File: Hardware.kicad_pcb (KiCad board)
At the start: 2 copper layers, 30.5 x 24 mm, 0 parts

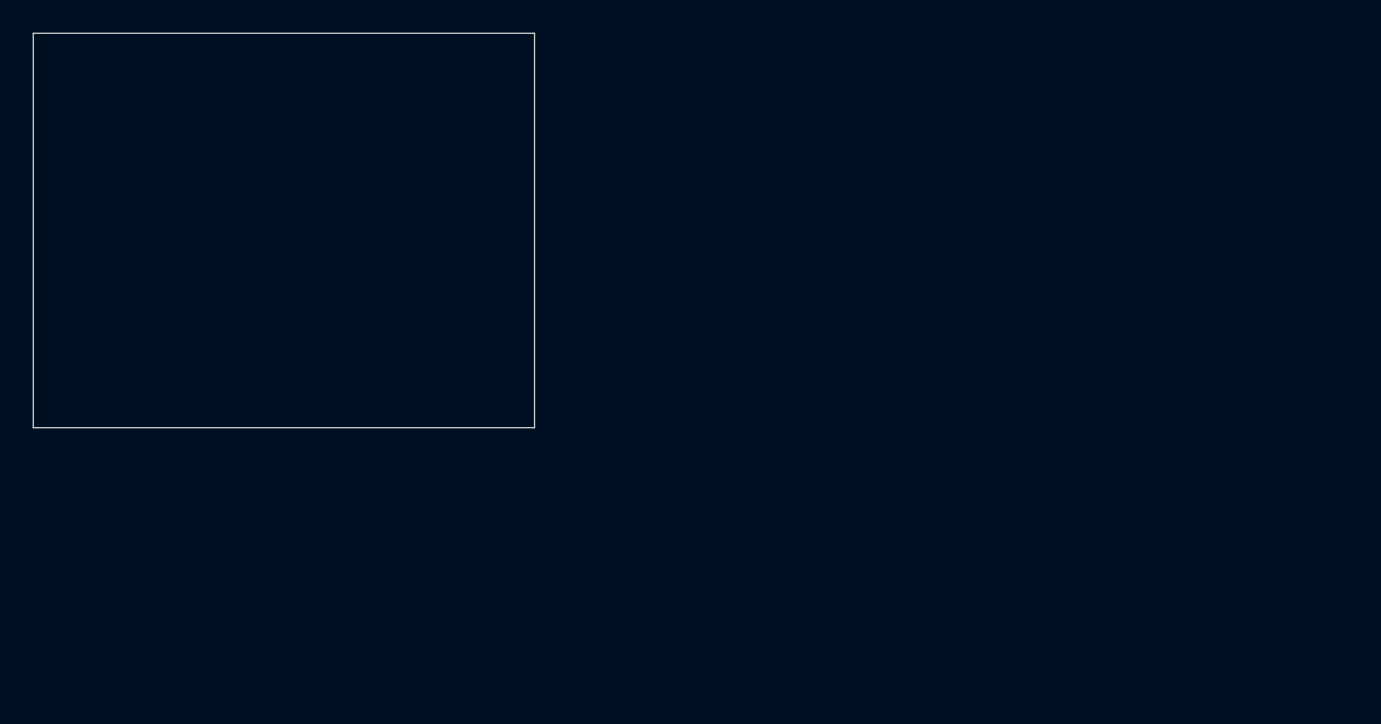
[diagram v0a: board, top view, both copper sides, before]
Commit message: added psu and formated board outline
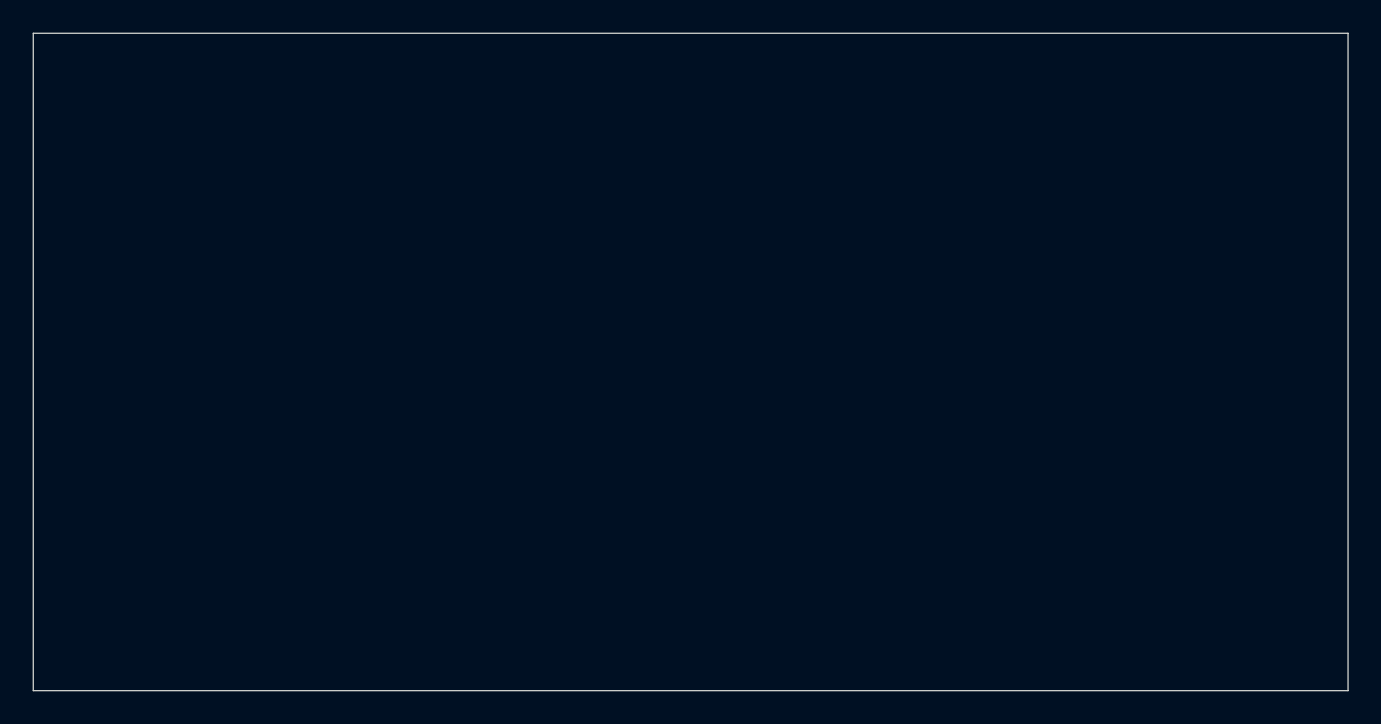
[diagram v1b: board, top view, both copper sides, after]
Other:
- board size 30.5 x 24 mm -> 80 x 40 mm
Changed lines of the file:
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@@
 	(gr_rect
 		(start 35.5 50)
-		(end 66 74)
+		(end 115.5 90)
 		(stroke
 			(width 0.05)

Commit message: finelized scematics
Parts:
- added BT1: Battery_Cell, Battery:BatteryHolder_Seiko_MS621F, F.Cu at (244.6, 128.6)
- added C1: 0.1uF, Capacitor_SMD:C_0805_2012Metric, F.Cu at (174.9, 100.5)
- added C10: NC, Capacitor_SMD:C_0805_2012Metric, F.Cu at (270.3, 86.3)
- added C11: NC, Capacitor_SMD:C_0805_2012Metric, F.Cu at (270.3, 89.3)
- added C14: 10uF, Capacitor_SMD:C_1206_3216Metric, F.Cu at (260.4, 86.4)
- added C17: 100pF, Capacitor_SMD:C_0805_2012Metric, F.Cu at (270.3, 92.3)
- added C18: 100pF, Capacitor_SMD:C_0805_2012Metric, F.Cu at (270.1, 111.4)
- added C19: 100pF, Capacitor_SMD:C_0805_2012Metric, F.Cu at (270.1, 114.4)
- added C2: 10uF, Capacitor_SMD:C_1206_3216Metric, F.Cu at (213.7, 100.7)
- added C20: 4.7uF, Capacitor_SMD:C_0805_2012Metric, F.Cu at (270.1, 117.4)
- added C21: 10uF, Capacitor_SMD:C_1206_3216Metric, F.Cu at (260.4, 89.8)
- added C22: 0.1uF, Capacitor_SMD:C_0805_2012Metric, F.Cu at (174.9, 112.6)
- added C23: 0.1uF, Capacitor_SMD:C_0805_2012Metric, F.Cu at (174.9, 115.6)
- added C24: 100pF, Capacitor_SMD:C_0805_2012Metric, F.Cu at (274.8, 86.3)
- added C25: 10uF, Capacitor_SMD:C_1206_3216Metric, F.Cu at (260.4, 93.1)
- added C26: 100pF, Capacitor_SMD:C_0805_2012Metric, F.Cu at (274.8, 89.3)
- added C27: 10uF, Capacitor_SMD:C_1206_3216Metric, F.Cu at (192.3, 132.1)
- added C28: 100pF, Capacitor_SMD:C_0805_2012Metric, F.Cu at (191.7, 138.6)
- added C29: 10uF, Capacitor_SMD:C_1206_3216Metric, F.Cu at (192.3, 135.4)
- added C3: 100pF, Capacitor_SMD:C_0805_2012Metric, F.Cu at (174.9, 103.5)
- added C30: 100pF, Capacitor_SMD:C_0805_2012Metric, F.Cu at (191.7, 141.6)
- added C31: 10uF, Capacitor_SMD:C_1206_3216Metric, F.Cu at (260.4, 96.5)
- added C32: 100pF, Capacitor_SMD:C_0805_2012Metric, F.Cu at (274.8, 92.3)
- added C33: 10uF, Capacitor_SMD:C_1206_3216Metric, F.Cu at (260.4, 99.8)
- added C34: 100pF, Capacitor_SMD:C_0805_2012Metric, F.Cu at (279.2, 86.3)
- added C35: 10uF, Capacitor_SMD:C_1206_3216Metric, F.Cu at (253.6, 127.5)
- added C36: 100pF, Capacitor_SMD:C_0805_2012Metric, F.Cu at (259.1, 121.3)
- added C37: 10uF, Capacitor_SMD:C_1206_3216Metric, F.Cu at (253.6, 130.9)
- added C38: 100pF, Capacitor_SMD:C_0805_2012Metric, F.Cu at (259.1, 124.3)
- added C39: 4.7uF, Capacitor_SMD:C_0805_2012Metric, F.Cu at (215.5, 123.6)
- added C4: 22uF, Capacitor_SMD:C_0603_1608Metric, F.Cu at (194.3, 100.3)
- added C40: 4.7uF, Capacitor_SMD:C_0805_2012Metric, F.Cu at (215.5, 126.6)
- added C41: 22uF, Capacitor_SMD:C_0603_1608Metric, F.Cu at (266.2, 58.0)
- added C42: 100pF, Capacitor_SMD:C_0805_2012Metric, F.Cu at (174.9, 118.6)
- added C43: 22uF, Capacitor_SMD:C_0603_1608Metric, F.Cu at (266.2, 60.5)
- added C44: 100pF, Capacitor_SMD:C_0805_2012Metric, F.Cu at (279.2, 89.3)
- added C45: 22uF, Capacitor_SMD:C_0603_1608Metric, F.Cu at (266.2, 63.0)
- added C46: 0.1uF, Capacitor_SMD:C_0805_2012Metric, F.Cu at (215.5, 129.6)
- added C47: 470pF, Capacitor_SMD:C_0603_1608Metric, F.Cu at (203.3, 123.3)
- added C48: 470pF, Capacitor_SMD:C_0603_1608Metric, F.Cu at (203.3, 125.8)
- added C49: 10uF, Capacitor_SMD:C_1206_3216Metric, F.Cu at (260.4, 103.2)
- added C5: 0.1uF, Capacitor_SMD:C_0805_2012Metric, F.Cu at (174.9, 106.5)
- added C50: 100pF, Capacitor_SMD:C_0805_2012Metric, F.Cu at (279.2, 92.3)
- added C51: 1uF, Capacitor_SMD:C_0603_1608Metric, F.Cu at (203.3, 128.4)
- added C6: 22uF, Capacitor_SMD:C_0603_1608Metric, F.Cu at (274.3, 114.7)
- added C7: 0.1uF, Capacitor_SMD:C_0805_2012Metric, F.Cu at (270.1, 108.4)
- added C8: 10uF, Capacitor_SMD:C_1206_3216Metric, F.Cu at (213.7, 104.0)
- added C9: 100pF, Capacitor_SMD:C_0805_2012Metric, F.Cu at (174.9, 109.5)
- added D1: LED, Capacitor_SMD:C_0603_1608Metric, F.Cu at (248.4, 125.7)
- added D10: BZV55B5V1, Diode_SMD:D_MiniMELF, F.Cu at (219.7, 100.7)
- added D12: 1N5819, Diode_THT:D_DO-41_SOD81_P10.16mm_Horizontal, F.Cu at (215.2, 139.8)
- added D2: 1N4148, Diode_THT:D_DO-35_SOD27_P7.62mm_Horizontal, F.Cu at (237.0, 134.6)
- added D3: PESD1CAN, Package_TO_SOT_SMD:SOT-23-3, F.Cu at (278.9, 122.5)
- added D4: LED, Capacitor_SMD:C_0603_1608Metric, F.Cu at (266.2, 65.5)
- added D5: LED, Capacitor_SMD:C_0603_1608Metric, F.Cu at (266.2, 68.0)
- added D6: BZV55B5V1, Diode_SMD:D_MiniMELF, F.Cu at (277.2, 82.0)
- added D7: LED, Capacitor_SMD:C_0603_1608Metric, F.Cu at (203.3, 130.9)
- added D8: LED, Capacitor_SMD:C_0603_1608Metric, F.Cu at (203.3, 133.4)
- added H1: MountingHole_Pad, MountingHole:MountingHole_3.2mm_M3_DIN965_Pad, F.Cu at (225.3, 60.3)
- added H2: MountingHole_Pad, MountingHole:MountingHole_3.2mm_M3_DIN965_Pad, F.Cu at (225.3, 67.4)
- added H3: MountingHole_Pad, MountingHole:MountingHole_3.2mm_M3_DIN965_Pad, F.Cu at (225.3, 74.6)
- added H4: MountingHole_Pad, MountingHole:MountingHole_3.2mm_M3_DIN965_Pad, F.Cu at (225.3, 81.7)
- added J1: Conn_01x06_Socket, Connector_PinHeader_2.54mm:PinHeader_1x06_P2.54mm_Vertical, F.Cu at (179.5, 101.3)
- added J2: JAE_SIM_Card_SF72S006, Connector_JAE:JAE_SIM_Card_SF72S006, F.Cu at (242.9, 90.7)
- added J3: Conn_Coaxial, Connector_Coaxial:U.FL_Molex_MCRF_73412-0110_Vertical, F.Cu at (253.8, 122.8)
- added J4: Conn_Coaxial, Connector_Coaxial:U.FL_Molex_MCRF_73412-0110_Vertical, F.Cu at (277.0, 77.3)
- added J5: Conn_01x05_Socket, Connector_PinHeader_2.54mm:PinHeader_1x05_P2.54mm_Vertical, F.Cu at (198.7, 101.3)
- added J6: Micro_SD_Card, Connector_Card:microSD_HC_Hirose_DM3BT-DSF-PEJS, F.Cu at (181.1, 131.4)
- added J9: Battery, Connector_JST:JST_PH_S2B-PH-SM4-TB_1x02-1MP_P2.00mm_Horizontal, F.Cu at (206.4, 140.3)
- added L1: 27uH, Inductor_SMD:L_0805_2012Metric, F.Cu at (253.1, 133.9)
- added L4: EPCO B82787C0513, EPCO_B82787C0513:EPCO B82787C0513, F.Cu at (278.8, 116.8)
- added L6: 220uH, Inductor_SMD:L_7.3x7.3_H4.5, F.Cu at (222.5, 126.5)
- added Q1: BC849, Package_TO_SOT_SMD:SOT-23, F.Cu at (203.4, 109.7)
- added Q2: BC849, Package_TO_SOT_SMD:SOT-23, F.Cu at (203.4, 114.4)
- added Q3: MMBT3904, Package_TO_SOT_SMD:SOT-23, F.Cu at (265.7, 87.2)
- added Q4: BC849, Package_TO_SOT_SMD:SOT-23, F.Cu at (265.7, 91.8)
- added Q5: MMBT3904, Package_TO_SOT_SMD:SOT-23, F.Cu at (265.7, 96.4)
- added Q6: MMBT3904, Package_TO_SOT_SMD:SOT-23, F.Cu at (265.7, 101.0)
- added R1: 10K, Resistor_SMD:R_0603_1608Metric, F.Cu at (194.3, 102.8)
- added R10: 60R, Resistor_SMD:R_0603_1608Metric, F.Cu at (274.3, 117.2)
- added R11: 60R, Resistor_SMD:R_0603_1608Metric, F.Cu at (274.3, 119.7)
- added R12: 120R, Resistor_SMD:R_0603_1608Metric, F.Cu at (248.4, 133.2)
- added R13: R33, Resistor_SMD:R_0603_1608Metric, F.Cu at (266.2, 70.5)
- added R17: 51R, Resistor_SMD:R_0603_1608Metric, F.Cu at (266.2, 73.0)
- added R18: 100K, Resistor_SMD:R_0603_1608Metric, F.Cu at (270.2, 58.0)
- added R19: 4K7, Resistor_SMD:R_0603_1608Metric, F.Cu at (270.2, 60.5)
- added R2: 1K, Resistor_SMD:R_0603_1608Metric, F.Cu at (207.3, 123.3)
- added R20: 4K7, Resistor_SMD:R_0603_1608Metric, F.Cu at (270.2, 63.0)
- added R21: 1k18, Resistor_SMD:R_0603_1608Metric, F.Cu at (207.3, 133.4)
- added R22: 10K, Resistor_SMD:R_0603_1608Metric, F.Cu at (194.3, 110.3)
- added R23: 3K9, Resistor_SMD:R_0603_1608Metric, F.Cu at (194.3, 112.8)
- added R24: 22R, Resistor_SMD:R_0603_1608Metric, F.Cu at (270.2, 65.5)
- added R25: 22R, Resistor_SMD:R_0603_1608Metric, F.Cu at (270.2, 68.0)
- added R26: 22R, Resistor_SMD:R_0603_1608Metric, F.Cu at (270.2, 70.5)
- added R29: 0.33R, Resistor_SMD:R_0603_1608Metric, F.Cu at (211.3, 123.3)
- added R3: 10K, Resistor_SMD:R_0603_1608Metric, F.Cu at (194.3, 105.3)
- added R30: 3K3, Resistor_SMD:R_0603_1608Metric, F.Cu at (211.3, 125.8)
- added R31: 1K2, Resistor_SMD:R_0603_1608Metric, F.Cu at (211.3, 128.4)
- added R4: 10K, Resistor_SMD:R_0603_1608Metric, F.Cu at (194.3, 107.8)
- added R41: 4K7, Resistor_SMD:R_0603_1608Metric, F.Cu at (270.2, 73.0)
- added R42: 47K, Resistor_SMD:R_0603_1608Metric, F.Cu at (274.2, 58.0)
- added R43: 51R, Resistor_SMD:R_0603_1608Metric, F.Cu at (274.2, 60.5)
- added R44: 1K, Resistor_SMD:R_0603_1608Metric, F.Cu at (274.2, 63.0)
- added R45: 1K, Resistor_SMD:R_0603_1608Metric, F.Cu at (274.2, 65.5)
- added R46: 4K7, Resistor_SMD:R_0603_1608Metric, F.Cu at (274.2, 68.0)
- added R47: 4K7, Resistor_SMD:R_0603_1608Metric, F.Cu at (274.2, 70.5)
- added R48: 100K, Resistor_SMD:R_0603_1608Metric, F.Cu at (274.2, 73.0)
- added R49: 4K7, Resistor_SMD:R_0603_1608Metric, F.Cu at (278.2, 58.0)
- added R5: 1K, Resistor_SMD:R_0603_1608Metric, F.Cu at (207.3, 125.8)
- added R50: 4K7, Resistor_SMD:R_0603_1608Metric, F.Cu at (278.2, 60.5)
- added R51: 22K, Resistor_SMD:R_0603_1608Metric, F.Cu at (278.2, 63.0)
- added R52: 10K, Resistor_SMD:R_0603_1608Metric, F.Cu at (278.2, 65.5)
- added R6: 10K, Resistor_SMD:R_0603_1608Metric, F.Cu at (207.3, 128.4)
- added R7: 1k13, Resistor_SMD:R_0603_1608Metric, F.Cu at (207.3, 130.9)
- added R8: 22R, Resistor_SMD:R_0603_1608Metric, F.Cu at (248.4, 128.2)
- added R9: 1K, Resistor_SMD:R_0603_1608Metric, F.Cu at (248.4, 130.7)
- added SW1: SW_Push, Button_Switch_THT:SW_PUSH_6mm, F.Cu at (183.8, 101.0)
- added SW3: SW_Push, Button_Switch_THT:SW_PUSH_6mm, F.Cu at (183.8, 109.6)
- added TP1: TestPoint, TestPoint:TestPoint_Pad_D2.0mm, F.Cu at (265.6, 109.1)
- added TP10: TestPoint, TestPoint:TestPoint_Pad_D2.0mm, F.Cu at (265.6, 122.8)
- added TP11: TestPoint, TestPoint:TestPoint_Pad_D2.0mm, F.Cu at (255.3, 87.0)
- added TP12: TestPoint, TestPoint:TestPoint_Pad_D2.0mm, F.Cu at (255.3, 91.6)
- added TP13: TestPoint, TestPoint:TestPoint_Pad_D2.0mm, F.Cu at (231.2, 63.5)
- added TP14: TestPoint, TestPoint:TestPoint_Pad_D2.0mm, F.Cu at (231.2, 68.1)
- added TP15: TestPoint, TestPoint:TestPoint_Pad_D2.0mm, F.Cu at (231.2, 72.6)
- added TP17: TestPoint, TestPoint:TestPoint_Pad_D2.0mm, F.Cu at (255.3, 96.1)
- added TP18: TestPoint, TestPoint:TestPoint_Pad_D2.0mm, F.Cu at (196.2, 139.4)
- added TP19: TestPoint, TestPoint:TestPoint_Pad_D2.0mm, F.Cu at (258.7, 132.7)
- added TP2: TestPoint, TestPoint:TestPoint_Pad_D2.0mm, F.Cu at (250.8, 87.0)
- added TP20: TestPoint, TestPoint:TestPoint_Pad_D2.0mm, F.Cu at (243.5, 147.9)
- added TP21: TestPoint, TestPoint:TestPoint_Pad_D2.0mm, F.Cu at (243.5, 152.5)
- added TP3: TestPoint, TestPoint:TestPoint_Pad_D2.0mm, F.Cu at (258.7, 128.1)
- added TP4: TestPoint, TestPoint:TestPoint_Pad_D2.0mm, F.Cu at (265.6, 113.7)
- added TP5: TestPoint, TestPoint:TestPoint_Pad_D2.0mm, F.Cu at (265.6, 118.2)
- added TP6: TestPoint, TestPoint:TestPoint_Pad_D2.0mm, F.Cu at (231.2, 59.0)
- added TP7: TestPoint, TestPoint:TestPoint_Pad_D2.0mm, F.Cu at (250.8, 91.6)
- added TP8: TestPoint, TestPoint:TestPoint_Pad_D2.0mm, F.Cu at (250.8, 96.1)
- added TP9: TestPoint, TestPoint:TestPoint_Pad_D2.0mm, F.Cu at (250.8, 100.7)
- added U1: ESP32-WROOM-32, RF_Module:ESP32-WROOM-32, F.Cu at (197.2, 88.0)
- added U10: MIC29302AWD, Package_TO_SOT_SMD:TO-252-5_TabPin3, F.Cu at (275.0, 97.8)
- added U11: AMS1117-3.3, Package_TO_SOT_SMD:SOT-223-3_TabPin2, F.Cu at (255.7, 111.1)
- added U13: MC34063AD, Package_SO:SOIC-8_3.9x4.9mm_P1.27mm, F.Cu at (217.5, 134.5)
- added U2: NEO-M8M, RF_GPS:ublox_NEO, F.Cu at (243.1, 115.6)
- added U3: SN65HVD231, Package_SO:SOIC-8_3.9x4.9mm_P1.27mm, F.Cu at (276.5, 110.2)
- added U4: BQ24075RGT, Package_DFN_QFN:VQFN-16-1EP_3x3mm_P0.5mm_EP1.6x1.6mm, F.Cu at (224.4, 133.8)
- added U5: AT24CS01-XHM, Package_SO:TSSOP-8_4.4x3mm_P0.65mm, F.Cu at (255.2, 117.5)
- added U6: A7670E, A7670E:A7670E, F.Cu at (250.1, 70.7)
- added U7: AMS1117-3.3, Package_TO_SOT_SMD:SOT-223-3_TabPin2, F.Cu at (205.9, 103.2)
- added U8: AMS1117-3.3, Package_TO_SOT_SMD:SOT-223-3_TabPin2, F.Cu at (194.4, 126.3)
- added U9: AMS1117-3.3, Package_TO_SOT_SMD:SOT-223-3_TabPin2, F.Cu at (269.1, 78.5)

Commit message: mostly layouted
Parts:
- C39, C40, C46, C47, C48, C51, D7, D8, J9, L6, R2, R21, R29, R30, R31, R5, R6, R7, U13, U4: moved to B.Cu
- D12: footprint Diode_THT:D_DO-41_SOD81_P10.16mm_Horizontal -> Diode_SMD:D_SOD-123; moved to B.Cu
- D2: footprint Diode_THT:D_DO-35_SOD27_P7.62mm_Horizontal -> Diode_SMD:D_SOD-323
- SW1, SW3: footprint Button_Switch_THT:SW_PUSH_6mm -> Jumper:SolderJumper-2_P1.3mm_Open_RoundedPad1.0x1.5mm
- moved U6 323.7 mm to (-73.5, 65.0)
- moved R18 315.6 mm to (-45.5, 55.2)
- moved R19 315.6 mm to (-45.5, 57.7)
- moved R20 315.6 mm to (-45.5, 60.2)
- moved R24 315.6 mm to (-45.5, 62.8)
- moved R25 315.6 mm to (-45.5, 65.3)
- moved R26 315.6 mm to (-45.5, 67.8)
- moved R41 315.6 mm to (-45.5, 70.3)
- moved U10 315.6 mm to (-40.6, 95.1)
- moved C14 315.6 mm to (-55.2, 83.7)
- moved C21 315.6 mm to (-55.2, 87.0)
- moved C24 315.6 mm to (-40.8, 83.5)
- moved C25 315.6 mm to (-55.2, 90.4)
- moved C26 315.6 mm to (-40.8, 86.5)
- moved C31 315.6 mm to (-55.2, 93.8)
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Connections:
- C18 pad 2: CAN_H -> CAN_L
- C19 pad 2: CAN_L -> CAN_H
- C51 pad 1: PW+ -> /PowerSupply_Module/StpDow_Out
- D3 pad 1: CAN_L -> CAN_H
- D3 pad 2: CAN_H -> CAN_L
- L4 pad 1: /CAN_Module/CANL -> /CAN_Module/CANH
- L4 pad 2: /CAN_Module/CANH -> /CAN_Module/CANL
- L4 pad 3: CAN_H -> CAN_L
- L4 pad 4: CAN_L -> CAN_H
- R10 pad 2: CAN_L -> CAN_H
- R11 pad 2: CAN_H -> CAN_L
- TP17 pad 1: GND -> /LTE_Module/3V3
- TP18 pad 1: GND -> /SD_Modula/PSU
- TP19 pad 1: GND -> /GPS_Module/PSU
- TP6 pad 1: GND -> /PSU
- U4 pad 13: PW+ -> /PowerSupply_Module/StpDow_Out
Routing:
- net /EN: track 0.00 -> 59.2 mm, vias 0 -> 3
- net +5V: track 0.00 -> 57.7 mm
- net GPS_RX: track 0.00 -> 42.4 mm
- net GPS_TX: track 0.00 -> 38.9 mm
- net /GPS_Module/PSU: track 0.00 -> 38.2 mm
- net /PSU: track 0.00 -> 27.9 mm
- net /ACC_Readout: track 0.00 -> 22.0 mm
- net Gps_V_Back: track 0.00 -> 20.8 mm
- net CAN_L: track 0.00 -> 20.1 mm
- net CAN_H: track 0.00 -> 19.2 mm
- net /GPS_Module/GPS_SCL: track 0.00 -> 17.3 mm
- net /PowerSupply_Module/StpDow_Out: track 0.00 -> 17.1 mm
- net /GPS_Module/GPS_SDA: track 0.00 -> 16.5 mm
- net /SD_Modula/PSU: track 0.00 -> 15.9 mm
- net PW+: track 0.00 -> 15.5 mm
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- added copper zone on B.Cu, net GND
- added copper zone on F.Cu, net GND

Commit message: pre remobing sd card
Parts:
- removed TP12, TP13, TP14, TP2, TP20, TP21, TP4, TP5: TestPoint, TestPoint:TestPoint_Pad_D2.0mm
- C14, C17, C21, C24, C27, C28, C29, C30, C41, C43, C44, C45, C49, C50, D4, D5, D6, J2, J6, Q3, Q4, Q5, Q6, R17, R18, R19, R20, R24, R25, R26, R41, R42, R43, R44, R45, R46, R47, R48, R49, R50, U6, U8: moved to B.Cu
- TP1, TP10, TP15, TP17, TP19, TP3, TP6: footprint TestPoint:TestPoint_Pad_D2.0mm -> TestPoint:TestPoint_Pad_D1.5mm
- TP11, TP18, TP7, TP8, TP9: footprint TestPoint:TestPoint_Pad_D2.0mm -> TestPoint:TestPoint_Pad_D1.5mm; moved to B.Cu
- moved C28 265.8 mm to (20.5, 134.6), turned to -90 degrees
- moved C27 261.0 mm to (20.5, 130.1)
- moved U8 252.8 mm to (25.5, 132.1)
- moved TP18 247.0 mm to (31.0, 141.1), turned to 180 degrees
- moved C30 245.3 mm to (30.5, 134.6), turned to -90 degrees
- moved C29 244.7 mm to (32.0, 131.6), turned to 0 degrees
- moved J6 225.8 mm to (41.7, 142.2), turned to 180 degrees
- moved C43 197.8 mm to (137.8, 121.3), turned to -90 degrees
- moved R24 191.5 mm to (137.8, 118.3), turned to -90 degrees
- moved R46 184.4 mm to (122.3, 150.0), turned to 180 degrees
- moved R47 184.4 mm to (122.3, 152.6), turned to 180 degrees
- moved R48 184.4 mm to (122.3, 155.1), turned to 180 degrees
- moved R49 177.3 mm to (118.3, 140.0), turned to 180 degrees
- moved R50 177.3 mm to (118.3, 142.5), turned to 180 degrees
- moved Q5 172.4 mm to (113.8, 147.4), turned to 180 degrees
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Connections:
- net /LTE_Module/CLK_EN renamed Net-(J2-CLK)
- net /LTE_Module/RST_EN renamed Net-(J2-RST)
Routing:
- net /ACC_Readout: track 22.0 -> 78.8 mm
- net /LTE_Module/1V8: track 0.00 -> 45.1 mm
- net CAN_TX: track 0.00 -> 41.0 mm
- net CAN_RX: track 0.00 -> 39.7 mm, vias 0 -> 2
- net /LTE_Module/SIM_VCC: track 0.00 -> 26.9 mm
- net /LTE_Module/VBAT: track 0.00 -> 24.2 mm
- net Net-(U6-I2C_SDA): track 0.00 -> 21.0 mm
- net Net-(U6-I2C_SCL): track 0.00 -> 20.0 mm
- net Net-(J2-RST): track 0.00 -> 15.5 mm
- net /SD_Modula/PSU: track 15.9 -> 30.5 mm
- net Net-(J2-CLK): track 0.00 -> 14.6 mm
- net ACC: track 0.00 -> 12.0 mm
- net /LTE_Module/S_DTR: track 0.00 -> 9.70 mm
- net Net-(U6-USB_DP): track 0.00 -> 9.69 mm
- net Net-(U6-USB_BOOT): track 0.00 -> 9.09 mm
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
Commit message: mostly finished layout
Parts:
- removed C27, C29: 10uF, Capacitor_SMD:C_1206_3216Metric
- removed C28, C30: 100pF, Capacitor_SMD:C_0805_2012Metric
- removed H3, H4: MountingHole_Pad, MountingHole:MountingHole_3.2mm_M3_DIN965_Pad
- removed J6: Micro_SD_Card, Connector_Card:microSD_HC_Hirose_DM3BT-DSF-PEJS
- removed TP17, TP18: TestPoint, TestPoint:TestPoint_Pad_D1.5mm
- removed U8: AMS1117-3.3, Package_TO_SOT_SMD:SOT-223-3_TabPin2
- added H5: MountingHole, MountingHole:MountingHole_3.2mm_M3, F.Cu at (111.0, 55.0)
- added H6: MountingHole, MountingHole:MountingHole_3.2mm_M3, F.Cu at (110.5, 85.0)
- C25, C26, C31, C32, C33, C34, R51, R52, U10, U9: moved to B.Cu
- moved C33 187.5 mm to (106.0, 63.4), turned to 180 degrees
- moved C25 182.1 mm to (105.5, 71.5), turned to 180 degrees
- moved C31 180.7 mm to (106.0, 82.0), turned to -90 degrees
- moved U10 174.1 mm to (103.5, 55.4), turned to 90 degrees
- moved C26 167.5 mm to (105.0, 69.0), turned to 180 degrees
- moved C32 166.9 mm to (106.0, 77.5), turned to 90 degrees
- moved C34 163.9 mm to (105.5, 65.9), turned to 180 degrees
- moved U9 162.6 mm to (100.0, 81.0), turned to 180 degrees
- moved R51 155.7 mm to (101.5, 62.9), turned to 180 degrees
- moved R52 154.7 mm to (99.0, 59.0), turned to 90 degrees
- moved C43 97.8 mm to (60.0, 62.0), turned to 180 degrees
- moved R24 96.9 mm to (60.0, 60.5), turned to 0 degrees
- moved R48 87.1 mm to (70.5, 85.0), turned to -90 degrees
- moved R47 84.2 mm to (72.0, 85.0), turned to -90 degrees
- moved R46 81.3 mm to (73.5, 85.0), turned to -90 degrees
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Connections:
- net /LTE_Module/DATA_EN renamed Net-(J2-I/O)
- TP11 pad 1: +5V -> Net-(U6-VBUS)
- U1 pad 30: SCK -> unconnected-(U1-IO18-Pad30)
- U1 pad 31: MISO -> unconnected-(U1-IO19-Pad31)
- U1 pad 33: SD_CS -> unconnected-(U1-IO21-Pad33)
- U1 pad 37: MOSI -> unconnected-(U1-IO23-Pad37)
- U6 pad 24: +5V -> Net-(U6-VBUS)
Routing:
- net +5V: track 59.6 -> 172.3 mm, vias 0 -> 3
- net /LTE_Module/3V3: track 6.35 -> 41.2 mm
- net LTE_RX: track 0.00 -> 31.2 mm, vias 0 -> 3
- net /SD_Modula/PSU: track 30.5 -> 0.00 mm
- net LTE_TX: track 0.00 -> 28.3 mm, vias 0 -> 3
- net /LTE_Module/VBAT: track 24.2 -> 45.5 mm
- net /LTE_Module/1V8: track 45.1 -> 59.5 mm
- net /GPS_Module/PSU: track 45.9 -> 59.7 mm
- net Net-(Q5-C): track 0.00 -> 12.7 mm
- net Net-(U6-I2C_SDA): track 21.0 -> 9.69 mm
- net Net-(J2-I/O): track 0.00 -> 10.3 mm
- net Net-(U6-VBUS): track 0.00 -> 9.35 mm
- net Net-(U6-I2C_SCL): track 20.0 -> 10.9 mm
- net /LTE_Module/SIM_VCC: track 26.9 -> 35.8 mm
- net Net-(Q6-E): track 0.00 -> 8.73 mm
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
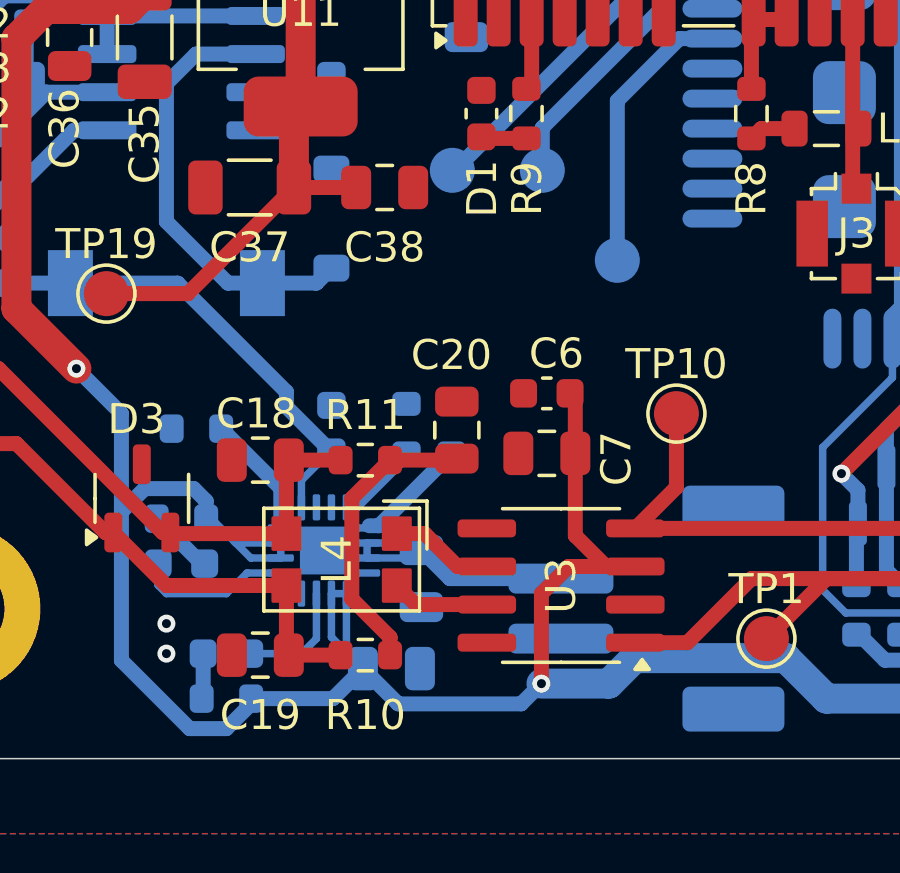
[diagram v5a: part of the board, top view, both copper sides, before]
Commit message: switchen can supply to 3v3
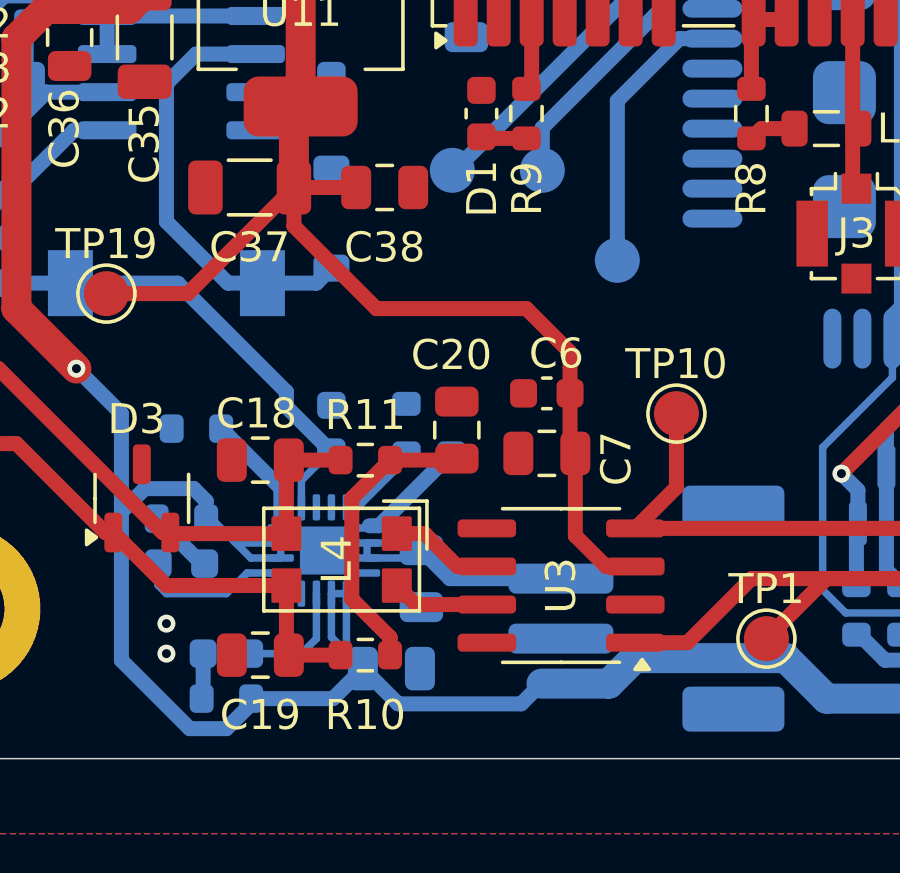
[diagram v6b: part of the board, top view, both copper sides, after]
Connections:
- C37 pad 1: /GPS_Module/PSU -> PSU_GPS
- C38 pad 1: /GPS_Module/PSU -> PSU_GPS
- C6 pad 1: +5V -> PSU_GPS
- C7 pad 1: +5V -> PSU_GPS
- D2 pad 2: /GPS_Module/PSU -> PSU_GPS
- TP19 pad 1: /GPS_Module/PSU -> PSU_GPS
- U11 pad 2: /GPS_Module/PSU -> PSU_GPS
- U2 pad 23: /GPS_Module/PSU -> PSU_GPS
- U3 pad 3: +5V -> PSU_GPS
- U5 pad 8: /GPS_Module/PSU -> PSU_GPS
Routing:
- net PSU_GPS: track 0.00 -> 80.5 mm
- net /GPS_Module/PSU: track 59.7 -> 0.00 mm
- net +5V: track 172.3 -> 159.8 mm, vias 3 -> 2
